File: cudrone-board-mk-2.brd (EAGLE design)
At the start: 100 x 70 mm, 139 parts, among them U1 EDISON_CONNECTOR_FULLMOUNTING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, U10 A2235-H, U11 FTS31XS-U, U12 BNO055, U2 FTS31XS-U, U4 TPS62065, U5 USD-SOCKETNEW, U6 TXB0108, U8 PCA9306, U9 PCA9306

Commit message: Changed the dspic to a slightly different version so we can use it with simulink coder
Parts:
- removed MOTOR_CONTROLLER: DSPIC33EP512MC806-I/PT, DSPIC33EP512MC806:TQFP64_10X10MC
- added U13: DSPIC33EP512MU810-X_PF, DSPIC33EP512MU810-IPF:TQFP100_14X14MC
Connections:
- new net VBUS: U13.54
- new net VDD_5: U13.46
- new net VDD_6: U13.62
- new net VSS_4: U13.45
- new net VSS_5: U13.65
- new net VUSB3V3: U13.55
- net AVDD: now also U13.30; no longer MOTOR_CONTROLLER.19
- net AVSS: now also U13.31; no longer MOTOR_CONTROLLER.20
- net VCAP: now also U13.85; no longer MOTOR_CONTROLLER.56
- net VDD: now also U13.86; no longer MOTOR_CONTROLLER.57
- net VDD_2: now also U13.2; no longer MOTOR_CONTROLLER.10
- net VDD_3: now also U13.16; no longer MOTOR_CONTROLLER.26
- net VDD_4: now also U13.37; no longer MOTOR_CONTROLLER.38
- net VSS: now also U13.75; no longer MOTOR_CONTROLLER.41
- net VSS_2: now also U13.15; no longer MOTOR_CONTROLLER.9
- net VSS_3: now also U13.36; no longer MOTOR_CONTROLLER.25
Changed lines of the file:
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@@
 </element>
 <element name="GIMBAL_SERVOS" library="Drone_Connectors" package="3X4" value="3X4" x="-69" y="-219"/>
-<element name="MOTOR_CONTROLLER" library="DSPIC33EP512MC806" package="TQFP64_10X10MC" value="DSPIC33EP512MC806-I/PT" x="-74" y="-278">
-<attribute name="VENDOR" value="MICROCHIP" x="-74" y="-278" size="1.778" layer="27" display="off"/>
-<attribute name="MANUFACTURER_PART_NUMBER" value="dspic33ep512mc806ipt" x="-74" y="-278" size="1.778" layer="27" display="off"/>
-</element>
 <element name="GIMBAL_SERVOS1" library="Drone_Connectors" package="3X4" value="3X4" x="-69" y="-297"/>
 <element name="ESC" library="Drone_Connectors" package="3X6" value="3X6" x="-66" y="-321"/>
@@
 <element name="R59" library="SparkFun-Resistors" package="0805" value="10k" x="-119" y="-681"/>
 <element name="R60" library="SparkFun-Resistors" package="0805" value="10k" x="-116" y="-681"/>
+<element name="U13" library="DSPIC33EP512MU810-IPF" package="TQFP100_14X14MC" value="DSPIC33EP512MU810-X_PF" x="-110" y="-693">
+<attribute name="MANUFACTURER_PART_NUMBER" value="dspic33ep512mu810-x_pf" x="-110" y="-693" size="1.778" layer="27" display="off"/>
+<attribute name="VENDOR" value="MICROCHIP" x="-110" y="-693" size="1.778" layer="27" display="off"/>
+</element>
 </elements>
 <signals>
@@
 <wire x1="-59.23" y1="-204.5692" x2="-66.85" y2="-210" width="0" layer="19" extent="1-1"/>
 </signal>
-<signal name="VSS_2">
-<contactref element="MOTOR_CONTROLLER" pad="9"/>
-</signal>
-<signal name="VDD_2">
-<contactref element="MOTOR_CONTROLLER" pad="10"/>
-</signal>
-<signal name="AVDD">
-<contactref element="MOTOR_CONTROLLER" pad="19"/>
-</signal>
-<signal name="AVSS">
-<contactref element="MOTOR_CONTROLLER" pad="20"/>
-</signal>
-<signal name="VSS_3">
-<contactref element="MOTOR_CONTROLLER" pad="25"/>
-</signal>
-<signal name="VDD_3">
-<contactref element="MOTOR_CONTROLLER" pad="26"/>
-</signal>
-<signal name="VDD_4">
-<contactref element="MOTOR_CONTROLLER" pad="38"/>
-</signal>
-<signal name="VSS">
-<contactref element="MOTOR_CONTROLLER" pad="41"/>
-</signal>
-<signal name="VCAP">
-<contactref element="MOTOR_CONTROLLER" pad="56"/>
-</signal>
-<signal name="VDD">
-<contactref element="MOTOR_CONTROLLER" pad="57"/>
-</signal>
 <signal name="PITCH">
 <contactref element="GIMBAL_SERVOS1" pad="S4"/>
@@
 <wire x1="-118.1" y1="-681" x2="-118" y2="-673.9" width="0" layer="19" extent="1-1"/>
 </signal>
+<signal name="VDD_2">
+<contactref element="U13" pad="2"/>
+</signal>
+<signal name="VSS_2">
+<contactref element="U13" pad="15"/>
+</signal>
+<signal name="VDD_3">
+<contactref element="U13" pad="16"/>
+</signal>
+<signal name="AVDD">
+<contactref element="U13" pad="30"/>
+</signal>
+<signal name="AVSS">
+<contactref element="U13" pad="31"/>
+</signal>
+<signal name="VSS_3">
+<contactref element="U13" pad="36"/>
+</signal>
+<signal name="VDD_4">
+<contactref element="U13" pad="37"/>
+</signal>
+<signal name="VSS_4">
+<contactref element="U13" pad="45"/>
+</signal>
+<signal name="VDD_5">
+<contactref element="U13" pad="46"/>
+</signal>
+<signal name="VBUS">
+<contactref element="U13" pad="54"/>
+</signal>
+<signal name="VUSB3V3">
+<contactref element="U13" pad="55"/>
+</signal>
+<signal name="VDD_6">
+<contactref element="U13" pad="62"/>
+</signal>
+<signal name="VSS_5">
+<contactref element="U13" pad="65"/>
+</signal>
+<signal name="VSS">
+<contactref element="U13" pad="75"/>
+</signal>
+<signal name="VCAP">
+<contactref element="U13" pad="85"/>
+</signal>
+<signal name="VDD">
+<contactref element="U13" pad="86"/>
+</signal>
 </signals>

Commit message: Added decoupling caps to mcu and isp pins
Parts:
- removed SJ4, SJ5: JUMPER-PAD-2-NC_BY_TRACE, SparkFun-Passives:PAD-JUMPER-2-NC_BY_TRACE_YES_SILK
- added C21, C22, C23, C24, C25, C27, C28: 0.1uF, SparkFun-Capacitors:0603-CAP
- added C26: 10uF, SparkFun-Capacitors:0603-CAP
- added ICSP: (no value), pinhead:1X06/90
- added R61: 10k, SparkFun-Resistors:0603
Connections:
- removed net AVDD: U13.30
- removed net AVSS: U13.31
- removed net N$33: R28.1, SJ5.2
- removed net VCAP: U13.85
- removed net VDD: U13.86
- removed net VDD_2: U13.2
- removed net VDD_3: U13.16
- removed net VDD_4: U13.37
- removed net VDD_5: U13.46
- removed net VDD_6: U13.62
- removed net VSS: U13.75
- removed net VSS_2: U13.15
- removed net VSS_3: U13.36
- removed net VSS_4: U13.45
- removed net VSS_5: U13.65
- new net LVP: ICSP.1
- new net PGC: ICSP.2, U13.26
- new net PGD: ICSP.3, U13.27
- new net VPP: ICSP.6, R61.1, U13.13
- net 3.3V: now also C21.2, C22.1, C23.1, C24.2, C25.1, C27.2, C28.1, ICSP.5, R61.2, U13.16, U13.2, U13.30, U13.37, U13.46, U13.62, U13.86
- net GND: now also C21.1, C22.2, C23.2, C24.1, C25.2, C26.1, C27.1, C28.2, ICSP.4, U13.15, U13.31, U13.36, U13.45, U13.65, U13.75
- net N$30: now also C26.2, U13.85; no longer SJ4.1, U11.17
- net N$31: now also R28.1; no longer SJ5.1
- net N$32: now also U11.17; no longer SJ4.2

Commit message: Connected i2c busses
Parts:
- removed SJ3: JUMPER-PAD-2-NC_BY_TRACE, SparkFun-Passives:PAD-JUMPER-2-NC_BY_TRACE_YES_SILK
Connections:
- removed net I2C0_SCL: U$4.P4, U$5.P4, U12.19
- removed net I2C0_SDA: U$4.P3, U$5.P3, U12.20
- removed net N$13: R5.1, SJ3.2
- net GND: now also R5.1; no longer SJ3.1
- net I2C_1_SCL: now also U$4.P4, U$5.P4, U12.19, U13.70
- net I2C_1_SDA: now also U$4.P3, U$5.P3, U12.20, U13.69
- net I2C_2_SCL: now also U13.58
- net I2C_2_SDA: now also U13.59

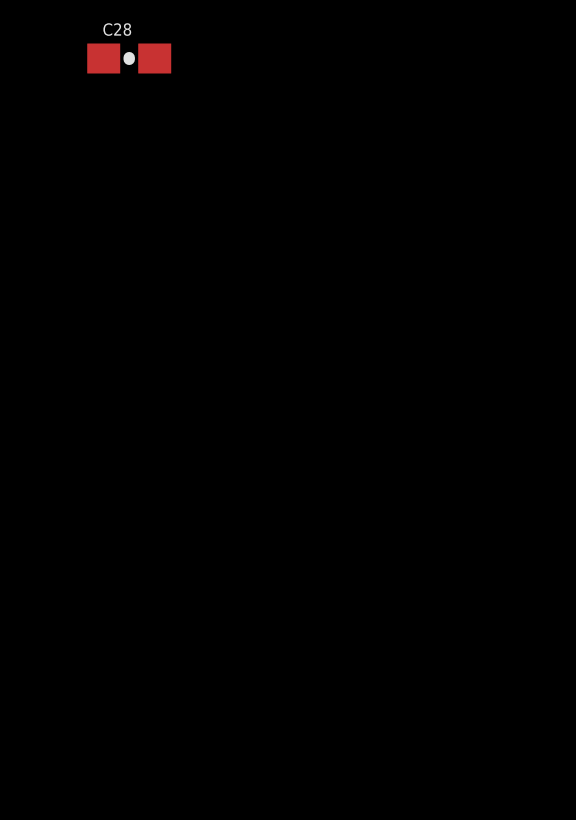
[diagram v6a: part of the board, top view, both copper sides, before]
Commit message: Made a few modifications in preparation of assigning pins on mcu
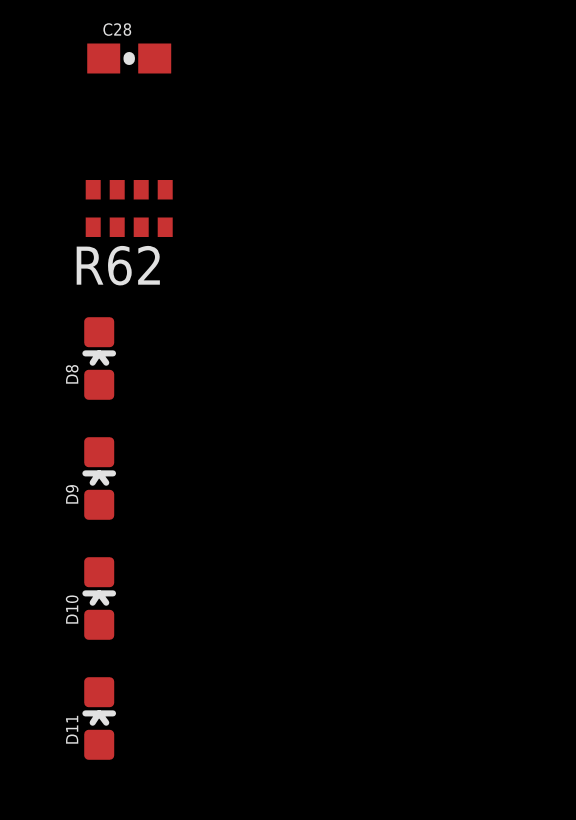
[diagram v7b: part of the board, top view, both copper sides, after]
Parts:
- added D10, D11, D8, D9: RED, SparkFun-LED:LED-0603
- added R62: 50, SparkFun-Passives:0603-ARV
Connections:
- new net MCU_LED_1: R62.8
- new net MCU_LED_2: R62.7
- new net MCU_LED_3: R62.6
- new net MCU_LED_4: R62.5
- new net N$13: D8.A, R62.4
- new net N$33: D9.A, R62.3
- new net N$43: D10.A, R62.2
- new net N$44: D11.A, R62.1
- net GND: now also D10.C, D11.C, D8.C, D9.C
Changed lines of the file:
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@@
 <attribute name="PROD_ID" value="CAP-00810" x="-121" y="-747" size="1.778" layer="27" display="off"/>
+</element>
+<element name="R62" library="SparkFun-Passives" package="0603-ARV" value="50" x="-121" y="-752"/>
+<element name="D8" library="SparkFun-LED" package="LED-0603" value="RED" x="-122" y="-757">
+<attribute name="PROD_ID" value="DIO-00819" x="-122" y="-757" size="1.778" layer="27" display="off"/>
+</element>
+<element name="D9" library="SparkFun-LED" package="LED-0603" value="RED" x="-122" y="-761">
+<attribute name="PROD_ID" value="DIO-00819" x="-122" y="-761" size="1.778" layer="27" display="off"/>
+</element>
+<element name="D10" library="SparkFun-LED" package="LED-0603" value="RED" x="-122" y="-765">
+<attribute name="PROD_ID" value="DIO-00819" x="-122" y="-765" size="1.778" layer="27" display="off"/>
+</element>
+<element name="D11" library="SparkFun-LED" package="LED-0603" value="RED" x="-122" y="-769">
+<attribute name="PROD_ID" value="DIO-00819" x="-122" y="-769" size="1.778" layer="27" display="off"/>
 </element>
 </elements>
@@
 <contactref element="U13" pad="65"/>
 <contactref element="R5" pad="1"/>
+<contactref element="D11" pad="C"/>
+<contactref element="D10" pad="C"/>
+<contactref element="D9" pad="C"/>
+<contactref element="D8" pad="C"/>
 <wire x1="-91.3175" y1="-412.3203" x2="-90.6825" y2="-417.6797" width="0" layer="19" extent="1-1"/>
 <wire x1="-98.275" y1="-418.3" x2="-90.6825" y2="-417.6797" width="0" layer="19" extent="1-1"/>
@@
 <wire x1="-64.1" y1="-82" x2="-66.85" y2="-91" width="0" layer="19" extent="1-1"/>
 <wire x1="-66" y1="-67" x2="-64.1" y2="-82" width="0" layer="19" extent="1-1"/>
-<wire x1="-103.25" y1="-526.4375" x2="-102.15" y2="-433" width="0" layer="19" extent="1-1"/>
+<wire x1="-94.05" y1="-526.025" x2="-102.15" y2="-433" width="0" layer="19" extent="1-1"/>
+<wire x1="-95.95" y1="-526.675" x2="-94.05" y2="-526.025" width="0" layer="19" extent="1-1"/>
+<wire x1="-100.6875" y1="-527.75" x2="-95.95" y2="-526.675" width="0" layer="19" extent="1-1"/>
+<wire x1="-100.6875" y1="-528.25" x2="-100.6875" y2="-527.75" width="0" layer="19" extent="1-1"/>
+<wire x1="-100.6875" y1="-528.75" x2="-100.6875" y2="-528.25" width="0" layer="19" extent="1-1"/>
+<wire x1="-100.75" y1="-529.5625" x2="-100.6875" y2="-528.75" width="0" layer="19" extent="1-1"/>
+<wire x1="-103.25" y1="-526.4375" x2="-100.6875" y2="-527.75" width="0" layer="19" extent="1-1"/>
 <wire x1="-105.3125" y1="-527.25" x2="-103.25" y2="-526.4375" width="0" layer="19" extent="1-1"/>
 <wire x1="-105.3125" y1="-528.75" x2="-105.3125" y2="-527.25" width="0" layer="19" extent="1-1"/>
 <wire x1="-105.25" y1="-529.5625" x2="-105.3125" y2="-528.75" width="0" layer="19" extent="1-1"/>
-<wire x1="-100.6875" y1="-527.75" x2="-103.25" y2="-526.4375" width="0" layer="19" extent="1-1"/>
-<wire x1="-100.6875" y1="-528.25" x2="-100.6875" y2="-527.75" width="0" layer="19" extent="1-1"/>
-<wire x1="-100.6875" y1="-528.75" x2="-100.6875" y2="-528.25" width="0" layer="19" extent="1-1"/>
-<wire x1="-100.75" y1="-529.5625" x2="-100.6875" y2="-528.75" width="0" layer="19" extent="1-1"/>
-<wire x1="-95.95" y1="-526.675" x2="-100.6875" y2="-527.75" width="0" layer="19" extent="1-1"/>
-<wire x1="-94.05" y1="-526.025" x2="-95.95" y2="-526.675" width="0" layer="19" extent="1-1"/>
 <wire x1="-98.15" y1="-534" x2="-100.75" y2="-529.5625" width="0" layer="19" extent="1-1"/>
 <wire x1="-96.15" y1="-538" x2="-98.15" y2="-534" width="0" layer="19" extent="1-1"/>
@@
 <wire x1="-121.85" y1="-744" x2="-121.85" y2="-741" width="0" layer="19" extent="1-1"/>
 <wire x1="-120.15" y1="-747" x2="-121.85" y2="-744" width="0" layer="19" extent="1-1"/>
+<wire x1="-122" y1="-756.123" x2="-120.15" y2="-747" width="0" layer="19" extent="1-1"/>
+<wire x1="-122" y1="-760.123" x2="-122" y2="-756.123" width="0" layer="19" extent="1-1"/>
+<wire x1="-122" y1="-764.123" x2="-122" y2="-760.123" width="0" layer="19" extent="1-1"/>
+<wire x1="-122" y1="-768.123" x2="-122" y2="-764.123" width="0" layer="19" extent="1-1"/>
 <wire x1="48.37" y1="47.02" x2="-66" y2="-67" width="0" layer="19" extent="1-1"/>
 <wire x1="48.77" y1="47.02" x2="48.37" y2="47.02" width="0" layer="19" extent="1-1"/>
@@
 <wire x1="-108.500003125" y1="-685.38" x2="-120.15" y2="-741" width="0" layer="19" extent="1-1"/>
 </signal>
+<signal name="N$13">
+<contactref element="D8" pad="A"/>
+<contactref element="R62" pad="4"/>
+<wire x1="-119.8" y1="-752.625" x2="-122" y2="-757.877" width="0" layer="19" extent="1-1"/>
+</signal>
+<signal name="N$33">
+<contactref element="D9" pad="A"/>
+<contactref element="R62" pad="3"/>
+<wire x1="-120.6" y1="-752.625" x2="-122" y2="-761.877" width="0" layer="19" extent="1-1"/>
+</signal>
+<signal name="N$43">
+<contactref element="D10" pad="A"/>
+<contactref element="R62" pad="2"/>
+<wire x1="-121.4" y1="-752.625" x2="-122" y2="-765.877" width="0" layer="19" extent="1-1"/>
+</signal>
+<signal name="N$44">
+<contactref element="D11" pad="A"/>
+<contactref element="R62" pad="1"/>
+<wire x1="-122.2" y1="-752.625" x2="-122" y2="-769.877" width="0" layer="19" extent="1-1"/>
+</signal>
+<signal name="MCU_LED_1">
+<contactref element="R62" pad="8"/>
+</signal>
+<signal name="MCU_LED_2">
+<contactref element="R62" pad="7"/>
+</signal>
+<signal name="MCU_LED_3">
+<contactref element="R62" pad="6"/>
+</signal>
+<signal name="MCU_LED_4">
+<contactref element="R62" pad="5"/>
+</signal>
 </signals>

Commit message: Added a bunch of tank capacitors
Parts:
- added C29: 0.1uF, SparkFun-Capacitors:0603-CAP
- added C30, C31, C32, C33, C34, C35, C36, C37, C38, C39, C40, C41, C42, C43, C44, C45, C46: 47 uF, SparkFun-Passives:0805
- C6: value 22uF -> 47 uF; device SparkFun-Capacitors:0805 -> SparkFun-Passives:0805
- moved C6 737.6 mm to (-138.0, -816.0)
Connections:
- removed net VUSB3V3: U13.55
- net 3.3V: now also C29.2, C30.1, C31.1, C32.1, C33.1, C34.1, C35.1, C36.1, C37.1, C38.1, C39.1, C40.1, C41.1, C42.1, C43.1, C44.1, C45.1, C46.1, U13.55
- net GND: now also C29.1, C30.2, C31.2, C32.2, C33.2, C34.2, C35.2, C36.2, C37.2, C38.2, C39.2, C40.2, C41.2, C42.2, C43.2, C44.2, C45.2, C46.2
